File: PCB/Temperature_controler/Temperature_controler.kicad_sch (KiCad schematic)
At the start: 0 parts

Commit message: PCB progress
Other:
- added sheet Power_supply_block (Power_supply_block.kicad_sch)
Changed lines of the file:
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@@
+	)
+	(sheet
+		(at 20.32 55.88)
+		(size 30.48 22.86)
+		(fields_autoplaced yes)
+		(stroke
+			(width 0.1524)
+			(type solid)
+		)
+		(fill
+			(color 0 0 0 0.0000)
+		)
+		(property "Sheetname" "Power_supply_block"
+			(at 20.32 55.1684 0)
+			(effects
+				(font
+					(size 1.27 1.27)
+				)
+				(justify left bottom)
+			)
+		)
+		(property "Sheetfile" "Power_supply_block.kicad_sch"
+			(at 20.32 79.3246 0)
+			(effects
+				(font
+					(size 1.27 1.27)
+				)
+				(justify left top)
+			)
+		)
+		(instances
+			(project "Temperature_controler"
+				(path "/e02f80f6-ce77-450b-a25c-ebd7c867a183"
+					(page "5")
+				)
+			)
+		)
 	)
 	(sheet

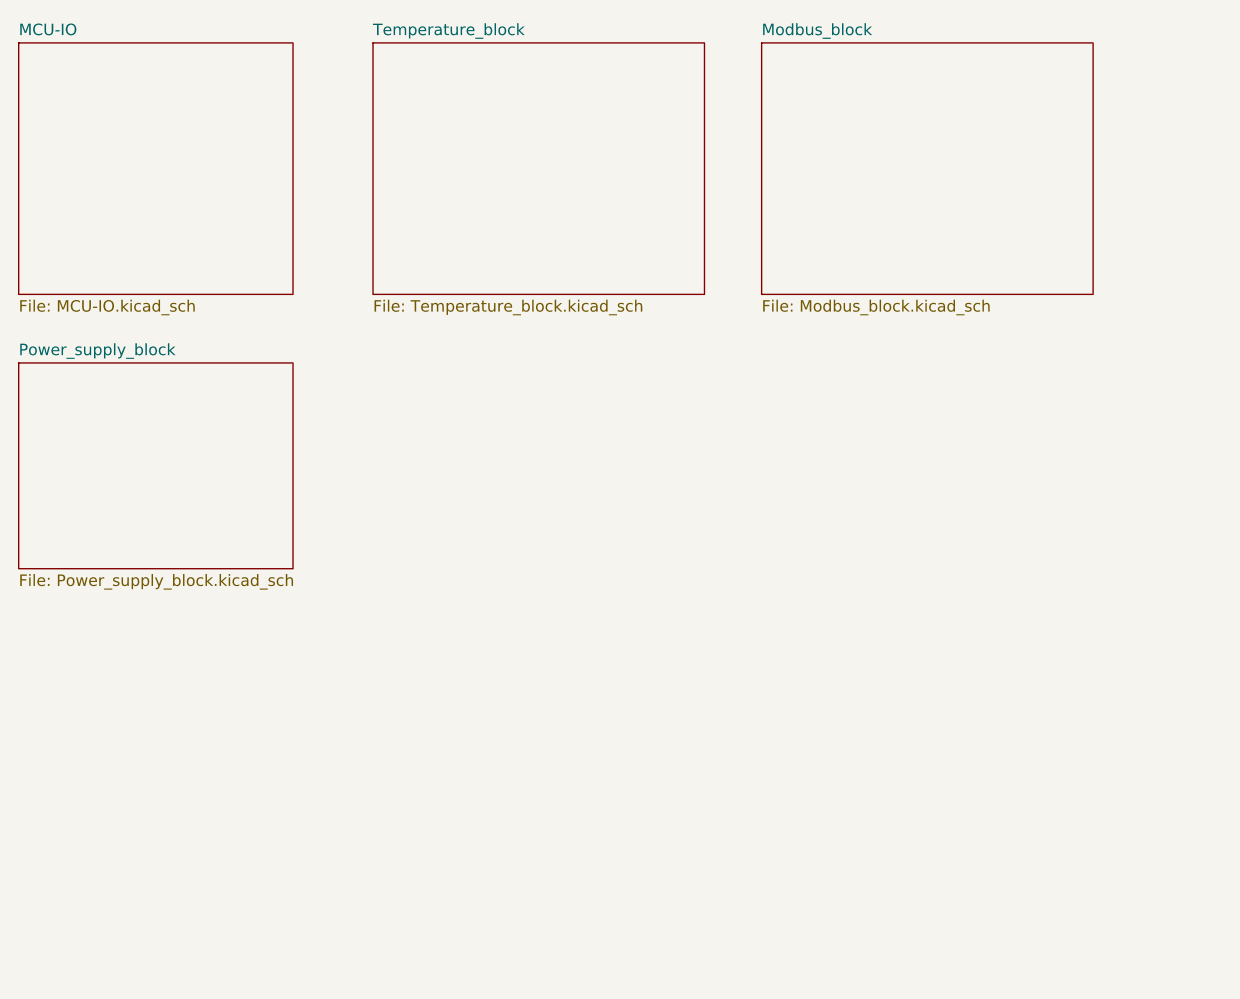
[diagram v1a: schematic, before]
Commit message: PCB layout progress and PDF for review added
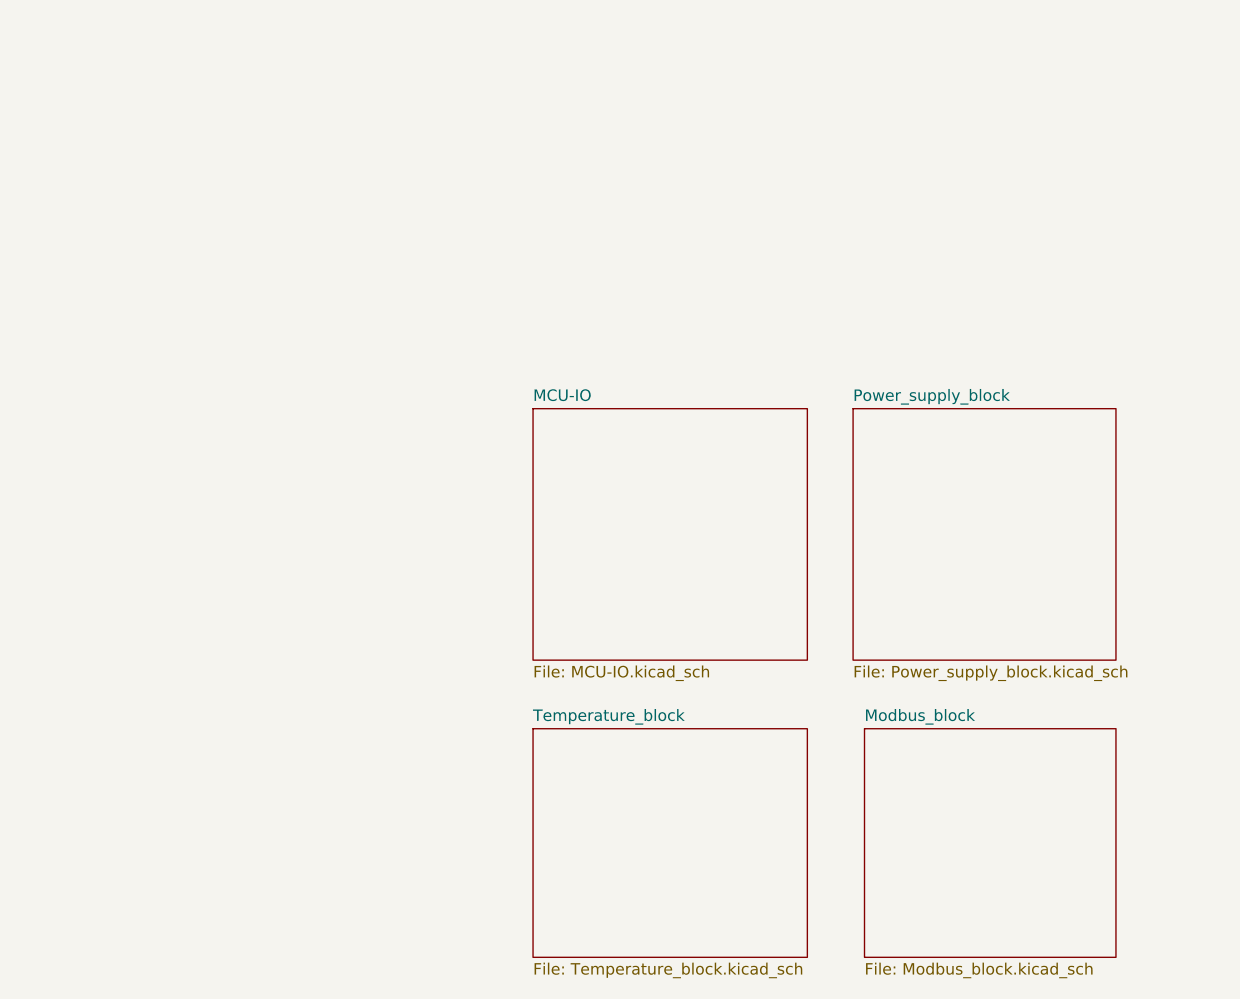
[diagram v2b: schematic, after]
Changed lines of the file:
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@@
 	(paper "A4")
 	(sheet
-		(at 20.32 20.32)
+		(at 77.47 60.96)
 		(size 30.48 27.94)
 		(fields_autoplaced yes)
@@
 		)
 		(property "Sheetname" "MCU-IO"
-			(at 20.32 19.6084 0)
+			(at 77.47 60.2484 0)
 			(effects
 				(font
@@
 		)
 		(property "Sheetfile" "MCU-IO.kicad_sch"
-			(at 20.32 48.8446 0)
+			(at 77.47 89.4846 0)
 			(effects
 				(font
@@
 	)
 	(sheet
-		(at 59.69 20.32)
-		(size 36.83 27.94)
+		(at 77.47 96.52)
+		(size 30.48 25.4)
 		(fields_autoplaced yes)
 		(stroke
@@
 		)
 		(property "Sheetname" "Temperature_block"
-			(at 59.69 19.6084 0)
+			(at 77.47 95.8084 0)
 			(effects
 				(font
@@
 		)
 		(property "Sheetfile" "Temperature_block.kicad_sch"
-			(at 59.69 48.8446 0)
+			(at 77.47 122.5046 0)
 			(effects
 				(font
@@
 	)
 	(sheet
-		(at 20.32 55.88)
-		(size 30.48 22.86)
+		(at 113.03 60.96)
+		(size 29.21 27.94)
 		(fields_autoplaced yes)
 		(stroke
@@
 		)
 		(property "Sheetname" "Power_supply_block"
-			(at 20.32 55.1684 0)
+			(at 113.03 60.2484 0)
 			(effects
 				(font
@@
 		)
 		(property "Sheetfile" "Power_supply_block.kicad_sch"
-			(at 20.32 79.3246 0)
+			(at 113.03 89.4846 0)
 			(effects
 				(font
@@
 	)
 	(sheet
-		(at 102.87 20.32)
-		(size 36.83 27.94)
+		(at 114.3 96.52)
+		(size 27.94 25.4)
 		(fields_autoplaced yes)
 		(stroke
@@
 		)
 		(property "Sheetname" "Modbus_block"
-			(at 102.87 19.6084 0)
+			(at 114.3 95.8084 0)
 			(effects
 				(font
@@
 		)
 		(property "Sheetfile" "Modbus_block.kicad_sch"
-			(at 102.87 48.8446 0)
+			(at 114.3 122.5046 0)
 			(effects
 				(font
